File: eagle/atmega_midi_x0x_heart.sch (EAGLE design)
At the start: 32 parts, among them IC1 TL072P, J11_VCF_CUTOFF 22-23-2021, U1 ATMEGA328P_PDIP

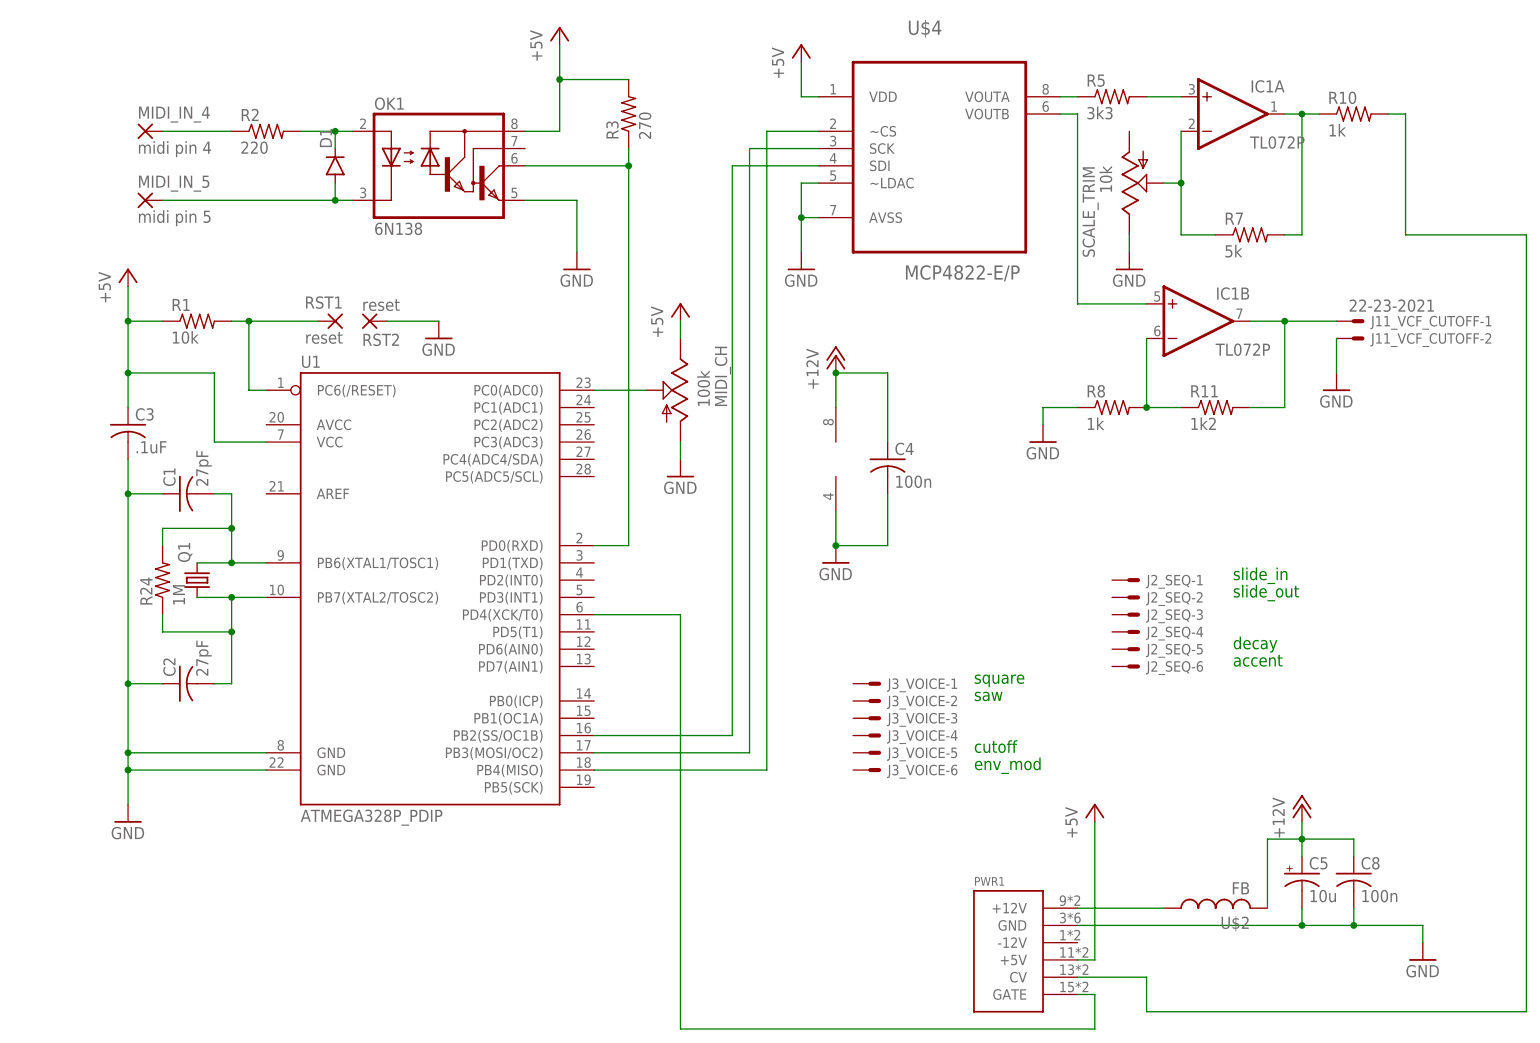
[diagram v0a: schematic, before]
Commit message: pwm pins connected in schemo
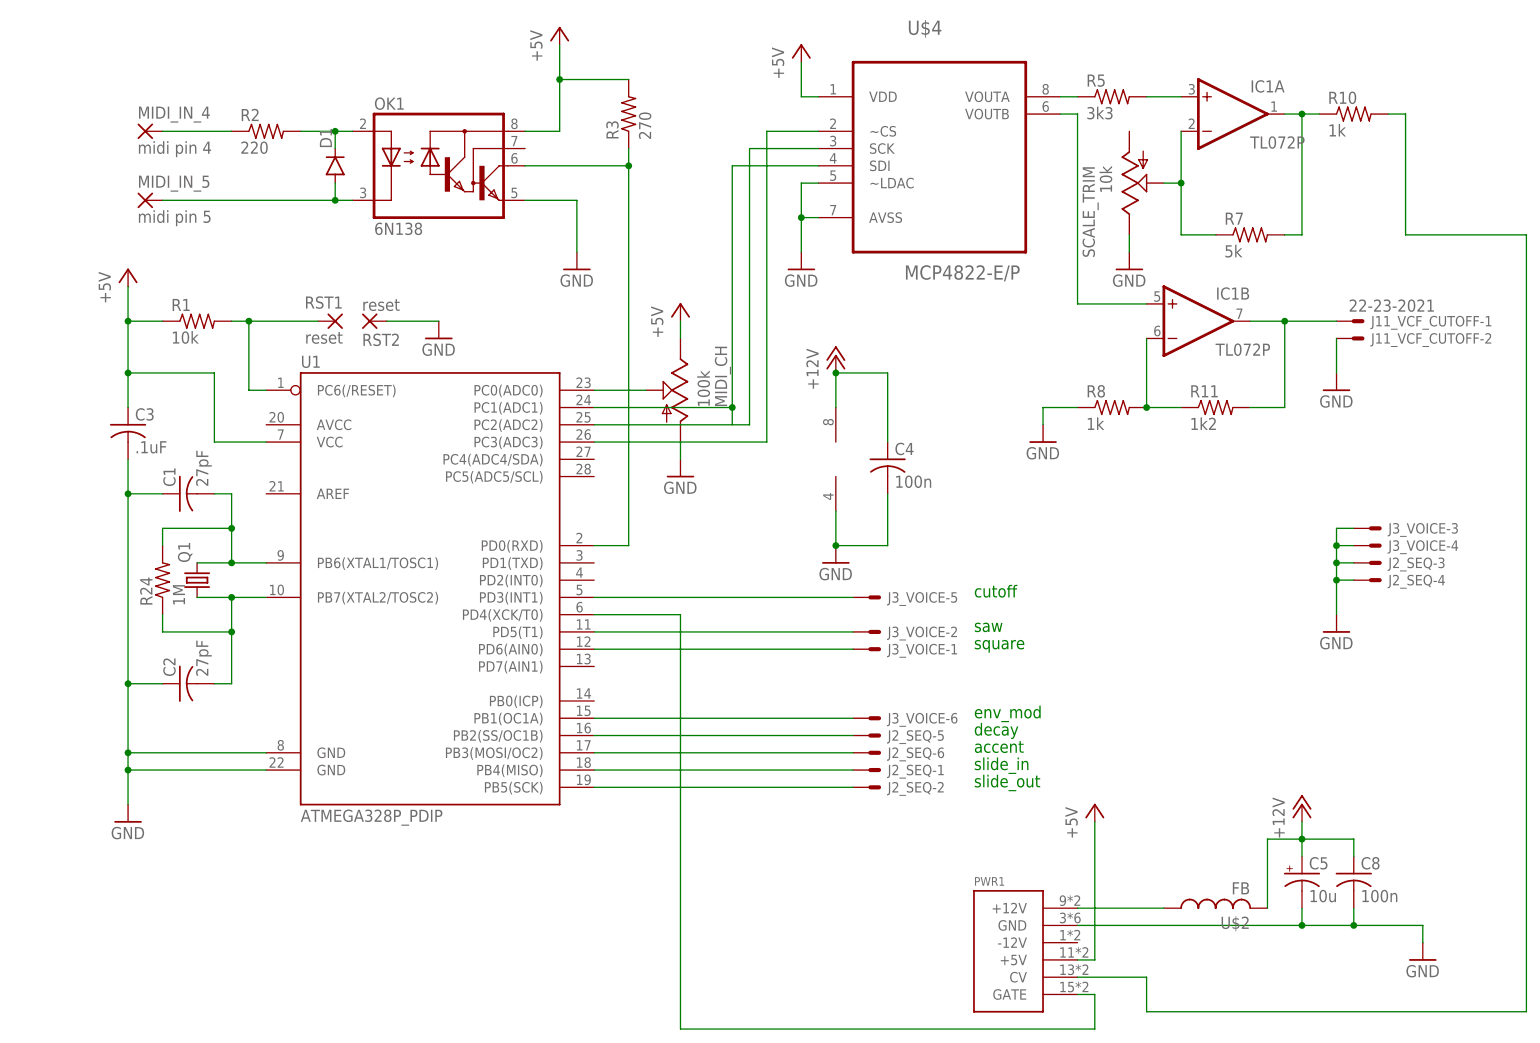
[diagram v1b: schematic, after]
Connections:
- new net N$1: J3_VOICE-5.S, U1.PD3(INT1)
- new net N$10: J3_VOICE-1.S, U1.PD6(AIN0)
- new net N$16: J3_VOICE-6.S, U1.PB1(OC1A)
- new net N$18: J2_SEQ-5.S, U1.PB2(SS/OC1B)
- new net N$20: J2_SEQ-6.S, U1.PB3(MOSI/OC2)
- new net N$21: J2_SEQ-1.S, U1.PB4(MISO)
- new net N$23: J2_SEQ-2.S, U1.PB5(SCK)
- new net N$9: J3_VOICE-2.S, U1.PD5(T1)
- net GND: now also J2_SEQ-3.S, J2_SEQ-4.S, J3_VOICE-3.S, J3_VOICE-4.S
- net N$25: now also U1.PC2(ADC2); no longer U1.PB3(MOSI/OC2)
- net N$26: now also U1.PC1(ADC1); no longer U1.PB2(SS/OC1B)
- net N$45: now also U1.PC3(ADC3); no longer U1.PB4(MISO)
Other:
- moved on the sheet: J2_SEQ-1, J2_SEQ-2, J2_SEQ-3, J2_SEQ-4, J2_SEQ-5, J2_SEQ-6, J3_VOICE-1, J3_VOICE-2, J3_VOICE-3, J3_VOICE-4, J3_VOICE-5, J3_VOICE-6
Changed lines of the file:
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@@
 <part name="J3_VOICE" library="con-molex" deviceset="22-23-2061" device=""/>
 <part name="J2_SEQ" library="con-molex" deviceset="22-23-2061" device=""/>
+<part name="GND11" library="supply1" deviceset="GND" device=""/>
 </parts>
 <sheets>
 <sheet>
 <plain>
-<text x="99.06" y="30.48" size="1.778" layer="91">square</text>
-<text x="99.06" y="27.94" size="1.778" layer="91">saw</text>
-<text x="99.06" y="20.32" size="1.778" layer="91">cutoff</text>
-<text x="99.06" y="17.78" size="1.778" layer="91">env_mod</text>
-<text x="137.16" y="45.72" size="1.778" layer="91">slide_in</text>
-<text x="137.16" y="43.18" size="1.778" layer="91">slide_out</text>
-<text x="137.16" y="35.56" size="1.778" layer="91">decay</text>
-<text x="137.16" y="33.02" size="1.778" layer="91">accent</text>
+<text x="99.06" y="35.56" size="1.778" layer="91">square</text>
+<text x="99.06" y="38.1" size="1.778" layer="91">saw</text>
+<text x="99.06" y="43.18" size="1.778" layer="91">cutoff</text>
+<text x="99.06" y="25.4" size="1.778" layer="91">env_mod</text>
+<text x="99.06" y="17.78" size="1.778" layer="91">slide_in</text>
+<text x="99.06" y="15.24" size="1.778" layer="91">slide_out</text>
+<text x="99.06" y="22.86" size="1.778" layer="91">decay</text>
+<text x="99.06" y="20.32" size="1.778" layer="91">accent</text>
 </plain>
 <instances>
@@
 <instance part="J11_VCF_CUTOFF" gate="-2" x="154.94" y="81.28"/>
 <instance part="GND3" gate="1" x="152.4" y="73.66"/>
-<instance part="J3_VOICE" gate="-1" x="83.82" y="30.48"/>
-<instance part="J3_VOICE" gate="-2" x="83.82" y="27.94"/>
-<instance part="J3_VOICE" gate="-3" x="83.82" y="25.4"/>
-<instance part="J3_VOICE" gate="-4" x="83.82" y="22.86"/>
-<instance part="J3_VOICE" gate="-5" x="83.82" y="20.32"/>
-<instance part="J3_VOICE" gate="-6" x="83.82" y="17.78"/>
-<instance part="J2_SEQ" gate="-1" x="121.92" y="45.72"/>
-<instance part="J2_SEQ" gate="-2" x="121.92" y="43.18"/>
-<instance part="J2_SEQ" gate="-3" x="121.92" y="40.64" smashed="yes">
-<attribute name="NAME" x="124.46" y="39.878" size="1.524" layer="95"/>
+<instance part="J3_VOICE" gate="-1" x="83.82" y="35.56"/>
+<instance part="J3_VOICE" gate="-2" x="83.82" y="38.1"/>
+<instance part="J3_VOICE" gate="-3" x="157.48" y="53.34"/>
+<instance part="J3_VOICE" gate="-4" x="157.48" y="50.8"/>
+<instance part="J3_VOICE" gate="-5" x="83.82" y="43.18"/>
+<instance part="J3_VOICE" gate="-6" x="83.82" y="25.4"/>
+<instance part="J2_SEQ" gate="-1" x="83.82" y="17.78"/>
+<instance part="J2_SEQ" gate="-2" x="83.82" y="15.24"/>
+<instance part="J2_SEQ" gate="-3" x="157.48" y="48.26" smashed="yes">
+<attribute name="NAME" x="160.02" y="47.498" size="1.524" layer="95"/>
 </instance>
-<instance part="J2_SEQ" gate="-4" x="121.92" y="38.1"/>
-<instance part="J2_SEQ" gate="-5" x="121.92" y="35.56"/>
-<instance part="J2_SEQ" gate="-6" x="121.92" y="33.02"/>
+<instance part="J2_SEQ" gate="-4" x="157.48" y="45.72"/>
+<instance part="J2_SEQ" gate="-5" x="83.82" y="22.86"/>
+<instance part="J2_SEQ" gate="-6" x="83.82" y="20.32"/>
+<instance part="GND11" gate="1" x="152.4" y="38.1"/>
 </instances>
 <busses>
@@
 <net name="N$25" class="0">
 <segment>
-<wire x1="66.04" y1="20.32" x2="66.04" y2="109.22" width="0.1524" layer="91"/>
 <pinref part="U$4" gate="A" pin="SCK"/>
+<wire x1="66.04" y1="68.58" x2="66.04" y2="109.22" width="0.1524" layer="91"/>
 <wire x1="66.04" y1="109.22" x2="76.2" y2="109.22" width="0.1524" layer="91"/>
-<pinref part="U1" gate="G$1" pin="PB3(MOSI/OC2)"/>
-<wire x1="66.04" y1="20.32" x2="43.18" y2="20.32" width="0.1524" layer="91"/>
+<pinref part="U1" gate="G$1" pin="PC2(ADC2)"/>
+<wire x1="43.18" y1="68.58" x2="66.04" y2="68.58" width="0.1524" layer="91"/>
 </segment>
 </net>
 <net name="N$26" class="0">
 <segment>
-<wire x1="63.5" y1="22.86" x2="63.5" y2="106.68" width="0.1524" layer="91"/>
 <pinref part="U$4" gate="A" pin="SDI"/>
+<wire x1="63.5" y1="71.12" x2="63.5" y2="106.68" width="0.1524" layer="91"/>
 <wire x1="63.5" y1="106.68" x2="76.2" y2="106.68" width="0.1524" layer="91"/>
-<pinref part="U1" gate="G$1" pin="PB2(SS/OC1B)"/>
-<wire x1="63.5" y1="22.86" x2="43.18" y2="22.86" width="0.1524" layer="91"/>
+<pinref part="U1" gate="G$1" pin="PC1(ADC1)"/>
+<wire x1="43.18" y1="71.12" x2="63.5" y2="71.12" width="0.1524" layer="91"/>
+<wire x1="63.5" y1="71.12" x2="63.5" y2="68.58" width="0.1524" layer="91"/>
+<junction x="63.5" y="71.12"/>
 </segment>
 </net>
@@
 <net name="N$45" class="0">
 <segment>
-<pinref part="U1" gate="G$1" pin="PB4(MISO)"/>
-<wire x1="43.18" y1="17.78" x2="68.58" y2="17.78" width="0.1524" layer="91"/>
 <pinref part="U$4" gate="A" pin="~CS"/>
-<wire x1="68.58" y1="17.78" x2="68.58" y2="111.76" width="0.1524" layer="91"/>
+<wire x1="68.58" y1="66.04" x2="68.58" y2="111.76" width="0.1524" layer="91"/>
 <wire x1="68.58" y1="111.76" x2="76.2" y2="111.76" width="0.1524" layer="91"/>
+<pinref part="U1" gate="G$1" pin="PC3(ADC3)"/>
+<wire x1="43.18" y1="66.04" x2="68.58" y2="66.04" width="0.1524" layer="91"/>
 </segment>
 </net>
@@
 <wire x1="152.4" y1="76.2" x2="152.4" y2="81.28" width="0.1524" layer="91"/>
 </segment>
-</net>
+<segment>
+<pinref part="J3_VOICE" gate="-3" pin="S"/>
+<pinref part="GND11" gate="1" pin="GND"/>
+<wire x1="154.94" y1="53.34" x2="152.4" y2="53.34" width="0.1524" layer="91"/>
+<wire x1="152.4" y1="53.34" x2="152.4" y2="50.8" width="0.1524" layer="91"/>
+<pinref part="J3_VOICE" gate="-4" pin="S"/>
+<wire x1="152.4" y1="50.8" x2="152.4" y2="48.26" width="0.1524" layer="91"/>
+<wire x1="152.4" y1="48.26" x2="152.4" y2="45.72" width="0.1524" layer="91"/>
+<wire x1="152.4" y1="45.72" x2="152.4" y2="40.64" width="0.1524" layer="91"/>
+<wire x1="154.94" y1="50.8" x2="152.4" y2="50.8" width="0.1524" layer="91"/>
+<junction x="152.4" y="50.8"/>
+<pinref part="J2_SEQ" gate="-3" pin="S"/>
+<wire x1="154.94" y1="48.26" x2="152.4" y2="48.26" width="0.1524" layer="91"/>
+<junction x="152.4" y="48.26"/>
+<pinref part="J2_SEQ" gate="-4" pin="S"/>
+<wire x1="154.94" y1="45.72" x2="152.4" y2="45.72" width="0.1524" layer="91"/>
+<junction x="152.4" y="45.72"/>
+</segment>
+</net>
+<net name="N$9" class="0">
+<segment>
+<pinref part="U1" gate="G$1" pin="PD5(T1)"/>
+<pinref part="J3_VOICE" gate="-2" pin="S"/>
+<wire x1="81.28" y1="38.1" x2="43.18" y2="38.1" width="0.1524" layer="91"/>
+</segment>
+</net>
+<net name="N$16" class="0">
+<segment>
+<pinref part="U1" gate="G$1" pin="PB1(OC1A)"/>
+<pinref part="J3_VOICE" gate="-6" pin="S"/>
+<wire x1="81.28" y1="25.4" x2="43.18" y2="25.4" width="0.1524" layer="91"/>
+</segment>
+</net>
+<net name="N$18" class="0">
+<segment>
+<pinref part="J2_SEQ" gate="-5" pin="S"/>
+<pinref part="U1" gate="G$1" pin="PB2(SS/OC1B)"/>
+<wire x1="81.28" y1="22.86" x2="43.18" y2="22.86" width="0.1524" layer="91"/>
+</segment>
+</net>
+<net name="N$20" class="0">
+<segment>
+<pinref part="J2_SEQ" gate="-6" pin="S"/>
+<pinref part="U1" gate="G$1" pin="PB3(MOSI/OC2)"/>
+<wire x1="81.28" y1="20.32" x2="43.18" y2="20.32" width="0.1524" layer="91"/>
+</segment>
+</net>
+<net name="N$21" class="0">
+<segment>
+<pinref part="J2_SEQ" gate="-1" pin="S"/>
+<pinref part="U1" gate="G$1" pin="PB4(MISO)"/>
+<wire x1="81.28" y1="17.78" x2="43.18" y2="17.78" width="0.1524" layer="91"/>
+</segment>
+</net>
+<net name="N$23" class="0">
+<segment>
+<pinref part="U1" gate="G$1" pin="PB5(SCK)"/>
+<pinref part="J2_SEQ" gate="-2" pin="S"/>
+<wire x1="43.18" y1="15.24" x2="81.28" y2="15.24" width="0.1524" layer="91"/>
+</segment>
+</net>
+<net name="N$1" class="0">
+<segment>
+<pinref part="J3_VOICE" gate="-5" pin="S"/>
+<pinref part="U1" gate="G$1" pin="PD3(INT1)"/>
+<wire x1="81.28" y1="43.18" x2="43.18" y2="43.18" width="0.1524" layer="91"/>
+</segment>
+</net>
+<net name="N$10" class="0">
+<segment>
+<pinref part="U1" gate="G$1" pin="PD6(AIN0)"/>
+<pinref part="J3_VOICE" gate="-1" pin="S"/>
+<wire x1="43.18" y1="35.56" x2="81.28" y2="35.56" width="0.1524" layer="91"/>
+</segment>
+</net>

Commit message: niced up schemo
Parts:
- removed MIDI_IN_4: midi pin 4, wirepad:2,54/0,9
- removed MIDI_IN_5: midi pin 5, wirepad:2,54/0,9
- added MIDI_IN: 22-23-2021, con-molex:22-23-2021
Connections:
- net N$3: now also MIDI_IN-2.S; no longer MIDI_IN_5.P
- net N$8: now also MIDI_IN-1.S; no longer MIDI_IN_4.P
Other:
- moved on the sheet: C4, C5, C8, D1, IC1A, IC1B, J11_VCF_CUTOFF-1, J11_VCF_CUTOFF-2, J2_SEQ-1, J2_SEQ-2, J2_SEQ-3, J2_SEQ-4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

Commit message: pretty good positioning
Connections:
- net N$1: now also J3_VOICE-6.S; no longer J3_VOICE-5.S
- net N$10: now also J3_VOICE-2.S; no longer J3_VOICE-1.S
- net N$16: now also J3_VOICE-5.S, U1.PD5(T1); no longer J3_VOICE-6.S, U1.PB1(OC1A)
- net N$18: now also J2_SEQ-1.S, U1.PB5(SCK); no longer J2_SEQ-5.S, U1.PB2(SS/OC1B)
- net N$20: now also J2_SEQ-2.S, U1.PB4(MISO); no longer J2_SEQ-6.S, U1.PB3(MOSI/OC2)
- net N$21: now also J2_SEQ-5.S, U1.PB3(MOSI/OC2); no longer J2_SEQ-1.S, U1.PB4(MISO)
- net N$23: now also J2_SEQ-6.S, U1.PB2(SS/OC1B); no longer J2_SEQ-2.S, U1.PB5(SCK)
- net N$9: now also J3_VOICE-1.S, U1.PB1(OC1A); no longer J3_VOICE-2.S, U1.PD5(T1)
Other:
- moved on the sheet: J2_SEQ-1, J2_SEQ-2, J2_SEQ-5, J2_SEQ-6, J3_VOICE-1, J3_VOICE-2, J3_VOICE-5, J3_VOICE-6
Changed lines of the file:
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@@
 <sheet>
 <plain>
-<text x="73.66" y="35.56" size="1.778" layer="91">square</text>
-<text x="73.66" y="38.1" size="1.778" layer="91">saw</text>
-<text x="73.66" y="43.18" size="1.778" layer="91">cutoff</text>
-<text x="73.66" y="25.4" size="1.778" layer="91">env_mod</text>
-<text x="73.66" y="17.78" size="1.778" layer="91">slide_in</text>
-<text x="73.66" y="15.24" size="1.778" layer="91">slide_out</text>
-<text x="73.66" y="22.86" size="1.778" layer="91">decay</text>
-<text x="73.66" y="20.32" size="1.778" layer="91">accent</text>
+<text x="73.66" y="25.4" size="1.778" layer="91">square</text>
+<text x="73.66" y="35.56" size="1.778" layer="91">saw</text>
+<text x="73.66" y="38.1" size="1.778" layer="91">cutoff</text>
+<text x="73.66" y="43.18" size="1.778" layer="91">env_mod</text>
+<text x="73.66" y="15.24" size="1.778" layer="91">slide_in</text>
+<text x="73.66" y="17.78" size="1.778" layer="91">slide_out</text>
+<text x="73.66" y="20.32" size="1.778" layer="91">decay</text>
+<text x="73.66" y="22.86" size="1.778" layer="91">accent</text>
 </plain>
 <instances>
@@
 <instance part="J11_VCF_CUTOFF" gate="-2" x="144.78" y="66.04"/>
 <instance part="GND3" gate="1" x="142.24" y="50.8"/>
-<instance part="J3_VOICE" gate="-1" x="58.42" y="35.56"/>
-<instance part="J3_VOICE" gate="-2" x="58.42" y="38.1"/>
+<instance part="J3_VOICE" gate="-1" x="58.42" y="25.4"/>
+<instance part="J3_VOICE" gate="-2" x="58.42" y="35.56"/>
 <instance part="J3_VOICE" gate="-3" x="96.52" y="40.64"/>
 <instance part="J3_VOICE" gate="-4" x="96.52" y="38.1"/>
-<instance part="J3_VOICE" gate="-5" x="58.42" y="43.18"/>
-<instance part="J3_VOICE" gate="-6" x="58.42" y="25.4"/>
-<instance part="J2_SEQ" gate="-1" x="58.42" y="17.78"/>
-<instance part="J2_SEQ" gate="-2" x="58.42" y="15.24"/>
+<instance part="J3_VOICE" gate="-5" x="58.42" y="38.1"/>
+<instance part="J3_VOICE" gate="-6" x="58.42" y="43.18"/>
+<instance part="J2_SEQ" gate="-1" x="58.42" y="15.24"/>
+<instance part="J2_SEQ" gate="-2" x="58.42" y="17.78"/>
 <instance part="J2_SEQ" gate="-3" x="96.52" y="35.56" smashed="yes">
 <attribute name="NAME" x="99.06" y="34.798" size="1.524" layer="95"/>
 </instance>
 <instance part="J2_SEQ" gate="-4" x="96.52" y="33.02"/>
-<instance part="J2_SEQ" gate="-5" x="58.42" y="22.86"/>
-<instance part="J2_SEQ" gate="-6" x="58.42" y="20.32"/>
+<instance part="J2_SEQ" gate="-5" x="58.42" y="20.32"/>
+<instance part="J2_SEQ" gate="-6" x="58.42" y="22.86"/>
 <instance part="GND11" gate="1" x="91.44" y="25.4"/>
 <instance part="MIDI_IN" gate="-1" x="-25.4" y="106.68" rot="MR0"/>
@@
 </segment>
 </net>
-<net name="N$9" class="0">
-<segment>
-<pinref part="U1" gate="G$1" pin="PD5(T1)"/>
-<pinref part="J3_VOICE" gate="-2" pin="S"/>
-<wire x1="55.88" y1="38.1" x2="43.18" y2="38.1" width="0.1524" layer="91"/>
-</segment>
-</net>
-<net name="N$16" class="0">
-<segment>
-<pinref part="U1" gate="G$1" pin="PB1(OC1A)"/>
-<pinref part="J3_VOICE" gate="-6" pin="S"/>
-<wire x1="55.88" y1="25.4" x2="43.18" y2="25.4" width="0.1524" layer="91"/>
-</segment>
-</net>
 <net name="N$18" class="0">
 <segment>
+<pinref part="J2_SEQ" gate="-1" pin="S"/>
+<pinref part="U1" gate="G$1" pin="PB5(SCK)"/>
+<wire x1="55.88" y1="15.24" x2="43.18" y2="15.24" width="0.1524" layer="91"/>
+</segment>
+</net>
+<net name="N$20" class="0">
+<segment>
+<pinref part="U1" gate="G$1" pin="PB4(MISO)"/>
+<pinref part="J2_SEQ" gate="-2" pin="S"/>
+<wire x1="43.18" y1="17.78" x2="55.88" y2="17.78" width="0.1524" layer="91"/>
+</segment>
+</net>
+<net name="N$21" class="0">
+<segment>
 <pinref part="J2_SEQ" gate="-5" pin="S"/>
-<pinref part="U1" gate="G$1" pin="PB2(SS/OC1B)"/>
-<wire x1="55.88" y1="22.86" x2="43.18" y2="22.86" width="0.1524" layer="91"/>
-</segment>
-</net>
-<net name="N$20" class="0">
-<segment>
-<pinref part="J2_SEQ" gate="-6" pin="S"/>
 <pinref part="U1" gate="G$1" pin="PB3(MOSI/OC2)"/>
 <wire x1="55.88" y1="20.32" x2="43.18" y2="20.32" width="0.1524" layer="91"/>
 </segment>
 </net>
-<net name="N$21" class="0">
-<segment>
-<pinref part="J2_SEQ" gate="-1" pin="S"/>
-<pinref part="U1" gate="G$1" pin="PB4(MISO)"/>
-<wire x1="55.88" y1="17.78" x2="43.18" y2="17.78" width="0.1524" layer="91"/>
-</segment>
-</net>
 <net name="N$23" class="0">
 <segment>
-<pinref part="U1" gate="G$1" pin="PB5(SCK)"/>
-<pinref part="J2_SEQ" gate="-2" pin="S"/>
-<wire x1="43.18" y1="15.24" x2="55.88" y2="15.24" width="0.1524" layer="91"/>
+<pinref part="U1" gate="G$1" pin="PB2(SS/OC1B)"/>
+<pinref part="J2_SEQ" gate="-6" pin="S"/>
+<wire x1="43.18" y1="22.86" x2="55.88" y2="22.86" width="0.1524" layer="91"/>
 </segment>
 </net>
 <net name="N$1" class="0">
 <segment>
-<pinref part="J3_VOICE" gate="-5" pin="S"/>
+<pinref part="J3_VOICE" gate="-6" pin="S"/>
 <pinref part="U1" gate="G$1" pin="PD3(INT1)"/>
 <wire x1="55.88" y1="43.18" x2="43.18" y2="43.18" width="0.1524" layer="91"/>
 </segment>
 </net>
+<net name="N$9" class="0">
+<segment>
+<pinref part="J3_VOICE" gate="-1" pin="S"/>
+<pinref part="U1" gate="G$1" pin="PB1(OC1A)"/>
+<wire x1="55.88" y1="25.4" x2="43.18" y2="25.4" width="0.1524" layer="91"/>
+</segment>
+</net>
 <net name="N$10" class="0">
 <segment>
+<pinref part="J3_VOICE" gate="-2" pin="S"/>
 <pinref part="U1" gate="G$1" pin="PD6(AIN0)"/>
-<pinref part="J3_VOICE" gate="-1" pin="S"/>
-<wire x1="43.18" y1="35.56" x2="55.88" y2="35.56" width="0.1524" layer="91"/>
-</segment>
-</net>
+<wire x1="55.88" y1="35.56" x2="43.18" y2="35.56" width="0.1524" layer="91"/>
+</segment>
+</net>
+<net name="N$16" class="0">
+<segment>
+<pinref part="U1" gate="G$1" pin="PD5(T1)"/>
+<pinref part="J3_VOICE" gate="-5" pin="S"/>
+<wire x1="43.18" y1="38.1" x2="55.88" y2="38.1" width="0.1524" layer="91"/>
+</segment>
+</net>

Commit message: rebuilt brd with redone gnd
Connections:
- removed net N$29: C1.1, C2.1, C3.2, C4.2, C5.-, C8.2, IC1P.V-, MIDI_CH.A, OK1.GND, PWR1.GND, R8.1, RST2.P, SCALE_TRIM.E, U$4.AVSS, U$4.~LDAC, U1.GND@1, U1.GND@2
- net GND: now also C1.1, C2.1, C3.2, C4.2, C5.-, C8.2, IC1P.V-, MIDI_CH.A, OK1.GND, PWR1.GND, R8.1, RST2.P, SCALE_TRIM.E, U$4.AVSS, U$4.~LDAC, U1.GND@1, U1.GND@2
